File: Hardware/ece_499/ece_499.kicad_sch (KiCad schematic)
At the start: 35 parts, among them J1 Conn_01x04, J2 Conn_01x04, J3 Conn_01x04, J4 Conn_01x04, Q1 DMN2004WK, Q2 DMN2004WK, Q3 DMN2004WK, Q4 DMN2004WK, SW1 RotaryEncoder_Switch, U1 Xiao ESP32-C3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

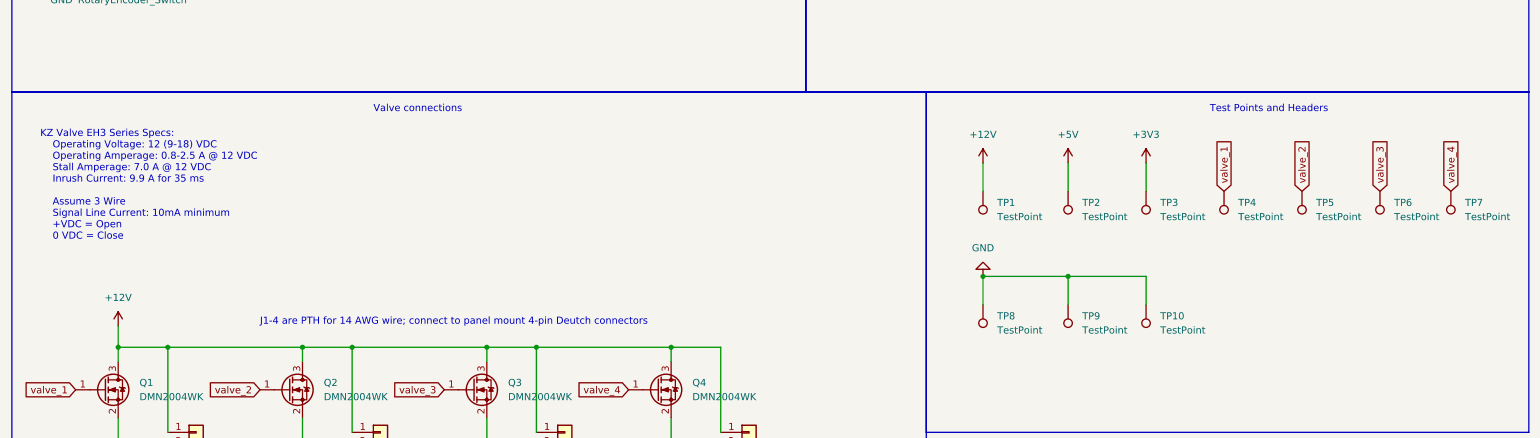
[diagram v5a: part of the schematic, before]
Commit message: Add debug LEDs to signal TPs
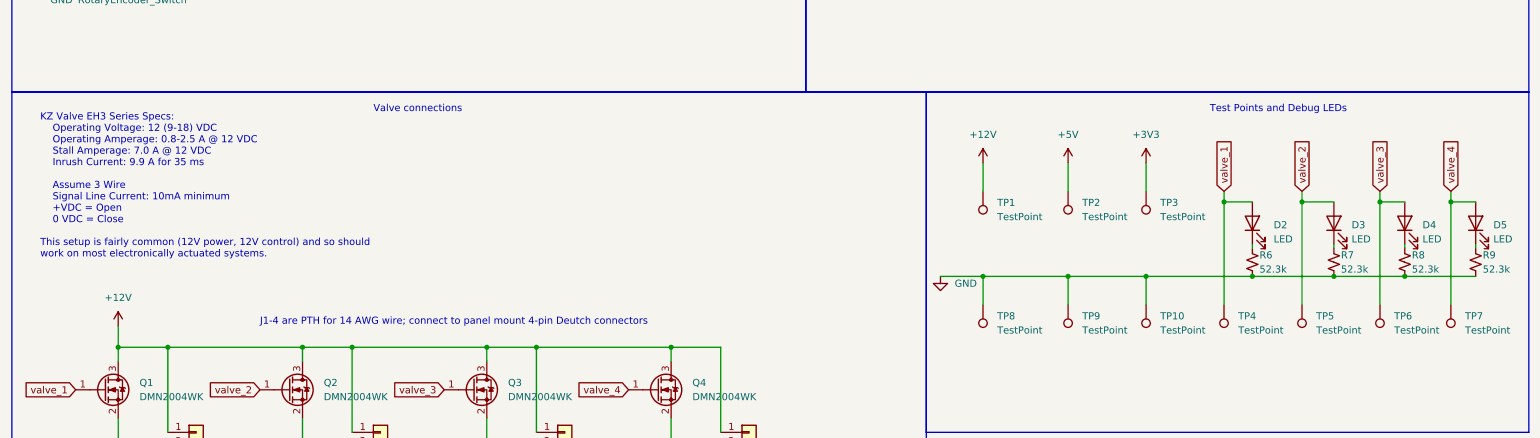
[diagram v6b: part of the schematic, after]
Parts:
- added D2, D3, D4, D5: LED, symbol Device:LED
- added R6, R7, R8, R9: 52.3k, symbol Device:R_Small_US
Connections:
- net GND: now also R6.2, R7.2, R8.2, R9.2
- net valve_1: now also D2.2 (A)
- net valve_2: now also D3.2 (A)
- net valve_3: now also D4.2 (A)
- net valve_4: now also D5.2 (A)
- new net: D2.1 (K), R6.1
- new net: D5.1 (K), R9.1
- new net: D3.1 (K), R7.1
- new net: D4.1 (K), R8.1
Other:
- note added: "KZ Valve EH3 Series Specs: Operating Voltage: 12 (9-18) VDC Operating Amperage: 0.8-2.5 A @ 12 VDC Stall Amperage: 7.0 A @ 12 VDC Inrush Current: 9.9 A for 35 ms Assume 3 Wire Signal Line Current: 10mA minimum +VDC = Open 0 VDC = Close This setup is fairly common (12V power, 12V control) and so should work on most electronically actuated systems."
- note added: "Test Points and Debug LEDs"
- note removed: "KZ Valve EH3 Series Specs: Operating Voltage: 12 (9-18) VDC Operating Amperage: 0.8-2.5 A @ 12 VDC Stall Amperage: 7.0 A @ 12 VDC Inrush Current: 9.9 A for 35 ms Assume 3 Wire Signal Line Current: 10mA minimum +VDC = Open 0 VDC = Close"
- note removed: "Test Points and Headers"
- moved on the sheet: TP4, TP5, TP6, TP7

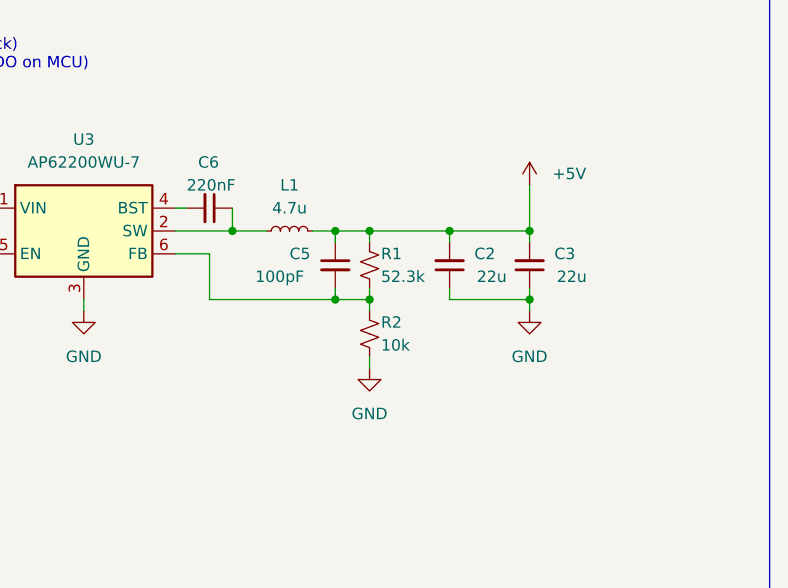
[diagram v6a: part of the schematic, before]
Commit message: Complete footprint selection
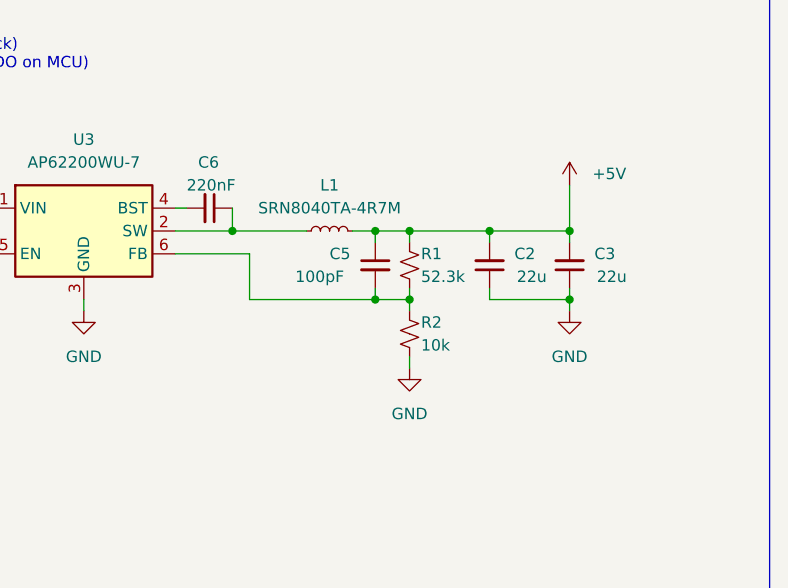
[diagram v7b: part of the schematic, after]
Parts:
- C1, C2, C3, C5, C6: footprint (none) -> Capacitor_SMD:C_0805_2012Metric_Pad1.18x1.45mm_HandSolder
- D2, D3, D4, D5: footprint (none) -> LED_THT:LED_D5.0mm
- J1, J2, J3, J4: footprint (none) -> Imported_Parts:14 AWG 01x04
- L1: value 4.7u -> SRN8040TA-4R7M; footprint (none) -> Imported_Parts:IND_SRN8040TA-4R7M
- R1, R2, R3, R4, R5: footprint (none) -> Resistor_SMD:R_1206_3216Metric_Pad1.30x1.75mm_HandSolder
- R6, R7, R8, R9: footprint (none) -> Resistor_THT:R_Axial_DIN0204_L3.6mm_D1.6mm_P5.08mm_Horizontal
- SW1: footprint (none) -> Resistor_SMD:R_0805_2012Metric_Pad1.20x1.40mm_HandSolder
- TP1, TP10, TP2, TP3, TP4, TP5, TP6, TP7, TP8, TP9: footprint (none) -> TestPoint:TestPoint_Pad_D2.0mm
- U4: footprint (none) -> Connector_PinHeader_1.00mm:PinHeader_1x06_P1.00mm_Horizontal
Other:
- moved on the sheet: C2, C3, C5, L1, R1, R2

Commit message: Remove incorrect encoder footprint; add main CANBUS header
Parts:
- added J5: Conn_01x04, Imported_Parts:14 AWG 01x04, symbol Connector_Generic:Conn_01x04
- SW1: footprint Resistor_SMD:R_0805_2012Metric_Pad1.20x1.40mm_HandSolder -> (none)
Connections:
- net +12V: now also J5.1 (Pin_1)
- net GND: now also J5.4 (Pin_4)
- net at U2.6 (CANL): now also J5.3 (Pin_3)
- net at U2.7 (CANH): now also J5.2 (Pin_2)
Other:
- note added: "Main connection to tractor/CANBUS (placeholder)"
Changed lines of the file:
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@@
+    (stroke (width 0) (type default))
+  )
+  (wire (pts (xy 134.62 47.625) (xy 134.62 53.34))
     (stroke (width 0) (type default))
   )
@@
     (stroke (width 0) (type default))
   )
+  (wire (pts (xy 121.92 58.42) (xy 121.92 60.96))
+    (stroke (width 0) (type default))
+  )
   (wire (pts (xy 26.67 58.42) (xy 31.75 58.42))
     (stroke (width 0) (type default))
@@
     (stroke (width 0) (type default))
   )
+  (wire (pts (xy 121.92 58.42) (xy 134.62 58.42))
+    (stroke (width 0) (type default))
+  )
   (wire (pts (xy 240.665 60.96) (xy 240.665 59.69))
     (stroke (width 0) (type default))
@@
     (stroke (width 0) (type default))
   )
+  (wire (pts (xy 134.62 60.96) (xy 134.62 63.5))
+    (stroke (width 0) (type default))
+  )
   (wire (pts (xy 36.83 58.42) (xy 49.53 58.42))
     (stroke (width 0) (type default))
   )
   (wire (pts (xy 274.955 131.445) (xy 274.955 132.08))
+    (stroke (width 0) (type default))
+  )
+  (wire (pts (xy 121.92 55.88) (xy 134.62 55.88))
     (stroke (width 0) (type default))
   )
@@
   (text "Can transciever converts from CAN_HI and CAN_LO to\nusable serial signals (and vice-versa)"
     (at 96.52 82.55 0)
+    (effects (font (size 1.27 1.27)) (justify left bottom))
+  )
+  (text "Main connection to\ntractor/CANBUS (placeholder)" (at 124.46 41.275 0)
     (effects (font (size 1.27 1.27)) (justify left bottom))
   )
@@
         (path "/3f2f140e-ca1f-4768-bf63-ce27bfebd1d1"
           (reference "#PWR06") (unit 1)
+        )
+      )
+    )
+  )
+  (symbol (lib_id "power:+12V") (at 134.62 47.625 0) (unit 1)
+    (in_bom yes) (on_board yes) (dnp no) (fields_autoplaced)
+    (property "Reference" "#PWR022" (at 134.62 51.435 0)
+      (effects (font (size 1.27 1.27)) hide)
+    )
+    (property "Value" "+12V" (at 134.62 42.545 0)
+      (effects (font (size 1.27 1.27)))
+    )
+    (property "Footprint" "" (at 134.62 47.625 0)
+      (effects (font (size 1.27 1.27)) hide)
+    )
+    (property "Datasheet" "" (at 134.62 47.625 0)
+      (effects (font (size 1.27 1.27)) hide)
+    )
+    (pin "1")
+    (instances
+      (project "ece_499"
+        (path "/3f2f140e-ca1f-4768-bf63-ce27bfebd1d1"
+          (reference "#PWR022") (unit 1)
         )
       )
@@
     )
   )
+  (symbol (lib_id "power:GND") (at 134.62 63.5 0) (unit 1)
+    (in_bom yes) (on_board yes) (dnp no) (fields_autoplaced)
+    (property "Reference" "#PWR023" (at 134.62 69.85 0)
+      (effects (font (size 1.27 1.27)) hide)
+    )
+    (property "Value" "GND" (at 134.62 68.58 0)
+      (effects (font (size 1.27 1.27)))
+    )
+    (property "Footprint" "" (at 134.62 63.5 0)
+      (effects (font (size 1.27 1.27)) hide)
+    )
+    (property "Datasheet" "" (at 134.62 63.5 0)
+      (effects (font (size 1.27 1.27)) hide)
+    )
+    (pin "1")
+    (instances
+      (project "ece_499"
+        (path "/3f2f140e-ca1f-4768-bf63-ce27bfebd1d1"
+          (reference "#PWR023") (unit 1)
+        )
+      )
+    )
+  )
   (symbol (lib_id "Device:LED") (at 234.95 127.635 90) (unit 1)
     (in_bom yes) (on_board yes) (dnp no) (fields_autoplaced)
@@
       (effects (font (size 1.27 1.27)))
     )
-    (property "Footprint" "Resistor_SMD:R_0805_2012Metric_Pad1.20x1.40mm_HandSolder" (at 30.48 73.406 0)
+    (property "Footprint" "" (at 30.48 73.406 0)
       (effects (font (size 1.27 1.27)) hide)
     )
@@
         )
       )
+    )
+  )
+  (symbol (lib_id "Connector_Generic:Conn_01x04") (at 139.7 55.88 0) (unit 1)
+    (in_bom yes) (on_board yes) (dnp no) (fields_autoplaced)
+    (property "Reference" "J5" (at 142.24 55.88 0)
+      (effects (font (size 1.27 1.27)) (justify left))
+    )
+    (property "Value" "Conn_01x04" (at 142.24 58.42 0)
+      (effects (font (size 1.27 1.27)) (justify left))
+    )
+    (property "Footprint" "Imported_Parts:14 AWG 01x04" (at 139.7 55.88 0)
+      (effects (font (size 1.27 1.27)) hide)
+    )
+    (property "Datasheet" "~" (at 139.7 55.88 0)
+      (effects (font (size 1.27 1.27)) hide)
+    )
+    (pin "3")
+    (pin "1")
+    (pin "2")
+    (pin "4")
+    (instances
+      (project "ece_499"
+        (path "/3f2f140e-ca1f-4768-bf63-ce27bfebd1d1"
+          (reference "J5") (unit 1)
+        )
+      )
